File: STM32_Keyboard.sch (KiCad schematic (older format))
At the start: 38 parts, among them U1 STM32F072CBTx, U2 SRV05-4, U3 MCP1700T-3302E_SOT23, Y1 8MHz

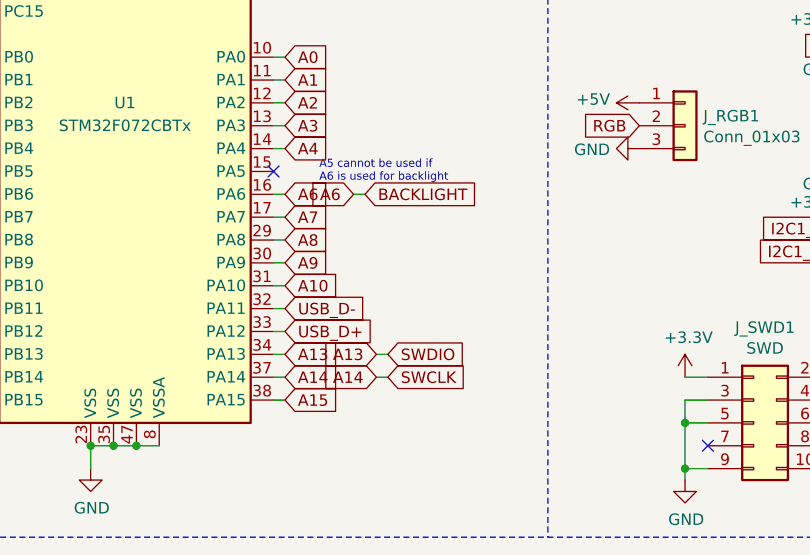
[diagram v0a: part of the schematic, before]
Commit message: Added 1.5kΩ USB D+ pull up resistor.
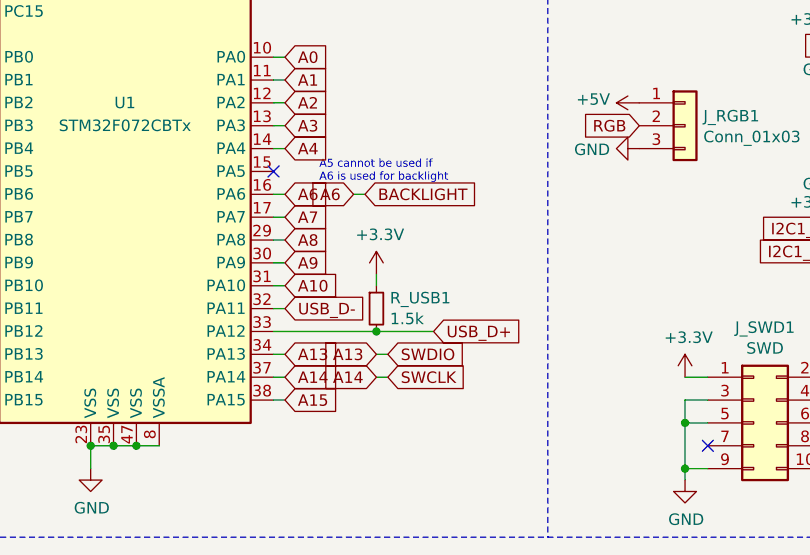
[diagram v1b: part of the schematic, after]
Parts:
- added R_USB1: 1.5k, Resistor_SMD:R_0603_1608Metric, symbol Device:R_Small
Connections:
- net +3V3: now also R_USB1.1
- net USB_D+: now also R_USB1.2
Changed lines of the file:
@@
 	2850 10200 2900 10200
 Wire Wire Line
-	2850 10300 2900 10300
+	2850 10300 3300 10300
 NoConn ~ 5250 10700
 NoConn ~ 5250 10800
@@
 Text GLabel 3350 10400 2    50   Input ~ 0
 SWDIO
-Text GLabel 2900 10300 2    50   Input ~ 0
+Text GLabel 3550 10300 2    50   Input ~ 0
 USB_D+
 Text GLabel 2900 10200 2    50   Input ~ 0
@@
 Wire Wire Line
 	4700 7300 4700 7850
+$Comp
+L Device:R_Small R_USB1
+U 1 1 5F9903E4
+P 3300 10200
+F 0 "R_USB1" H 3359 10246 50  0000 L CNN
+F 1 "1.5k" H 3359 10155 50  0000 L CNN
+F 2 "Resistor_SMD:R_0603_1608Metric" H 3300 10200 50  0001 C CNN
+F 3 "~" H 3300 10200 50  0001 C CNN
+	1    3300 10200
+	1    0    0    -1
+$EndComp
+Connection ~ 3300 10300
+Wire Wire Line
+	3300 10300 3550 10300
+Wire Wire Line
+	3300 10100 3300 10050
+$Comp
+L power:+3.3V #PWR0121
+U 1 1 5F99C5A7
+P 3300 10050
+F 0 "#PWR0121" H 3300 9900 50  0001 C CNN
+F 1 "+3.3V" H 3315 10223 50  0000 C CNN
+F 2 "" H 3300 10050 50  0001 C CNN
+F 3 "" H 3300 10050 50  0001 C CNN
+	1    3300 10050
+	1    0    0    -1
+$EndComp
 $EndSCHEMATC
